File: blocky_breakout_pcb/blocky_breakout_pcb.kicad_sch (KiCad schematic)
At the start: 5 parts, among them J12 Conn_01x02_Pin

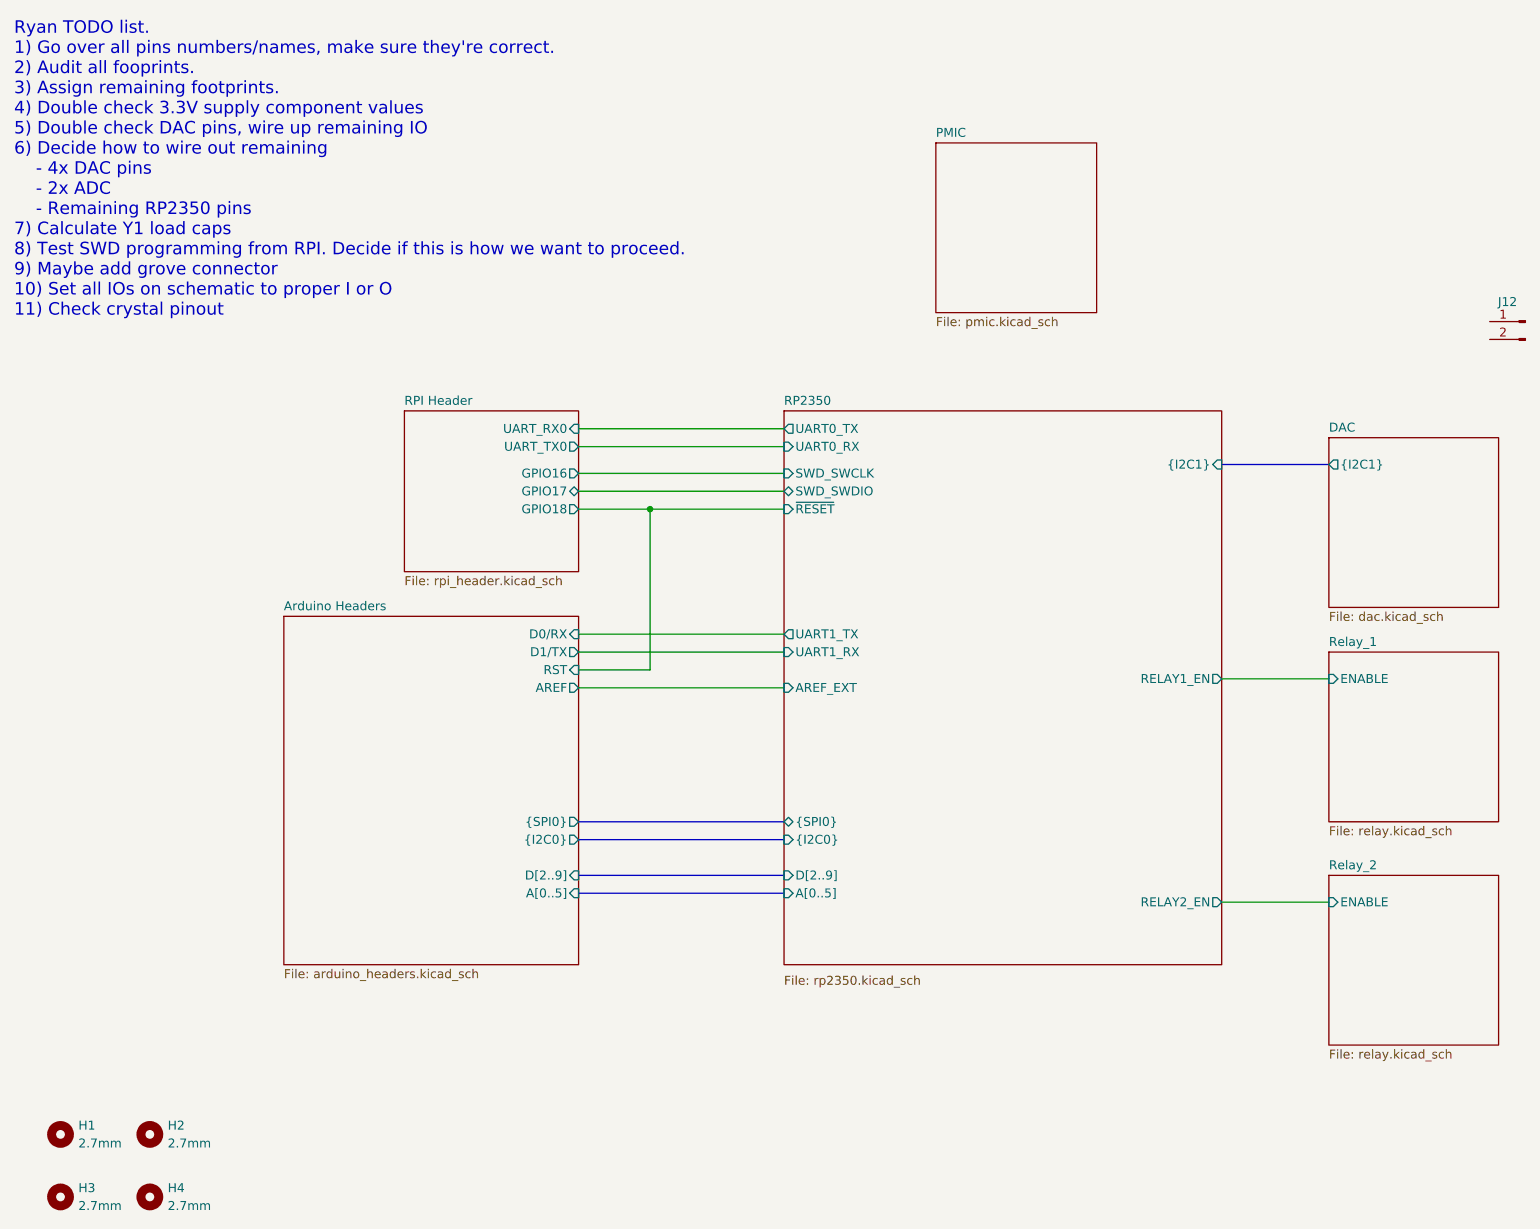
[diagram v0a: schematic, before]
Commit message: Layout nearly finished, entering part numbers
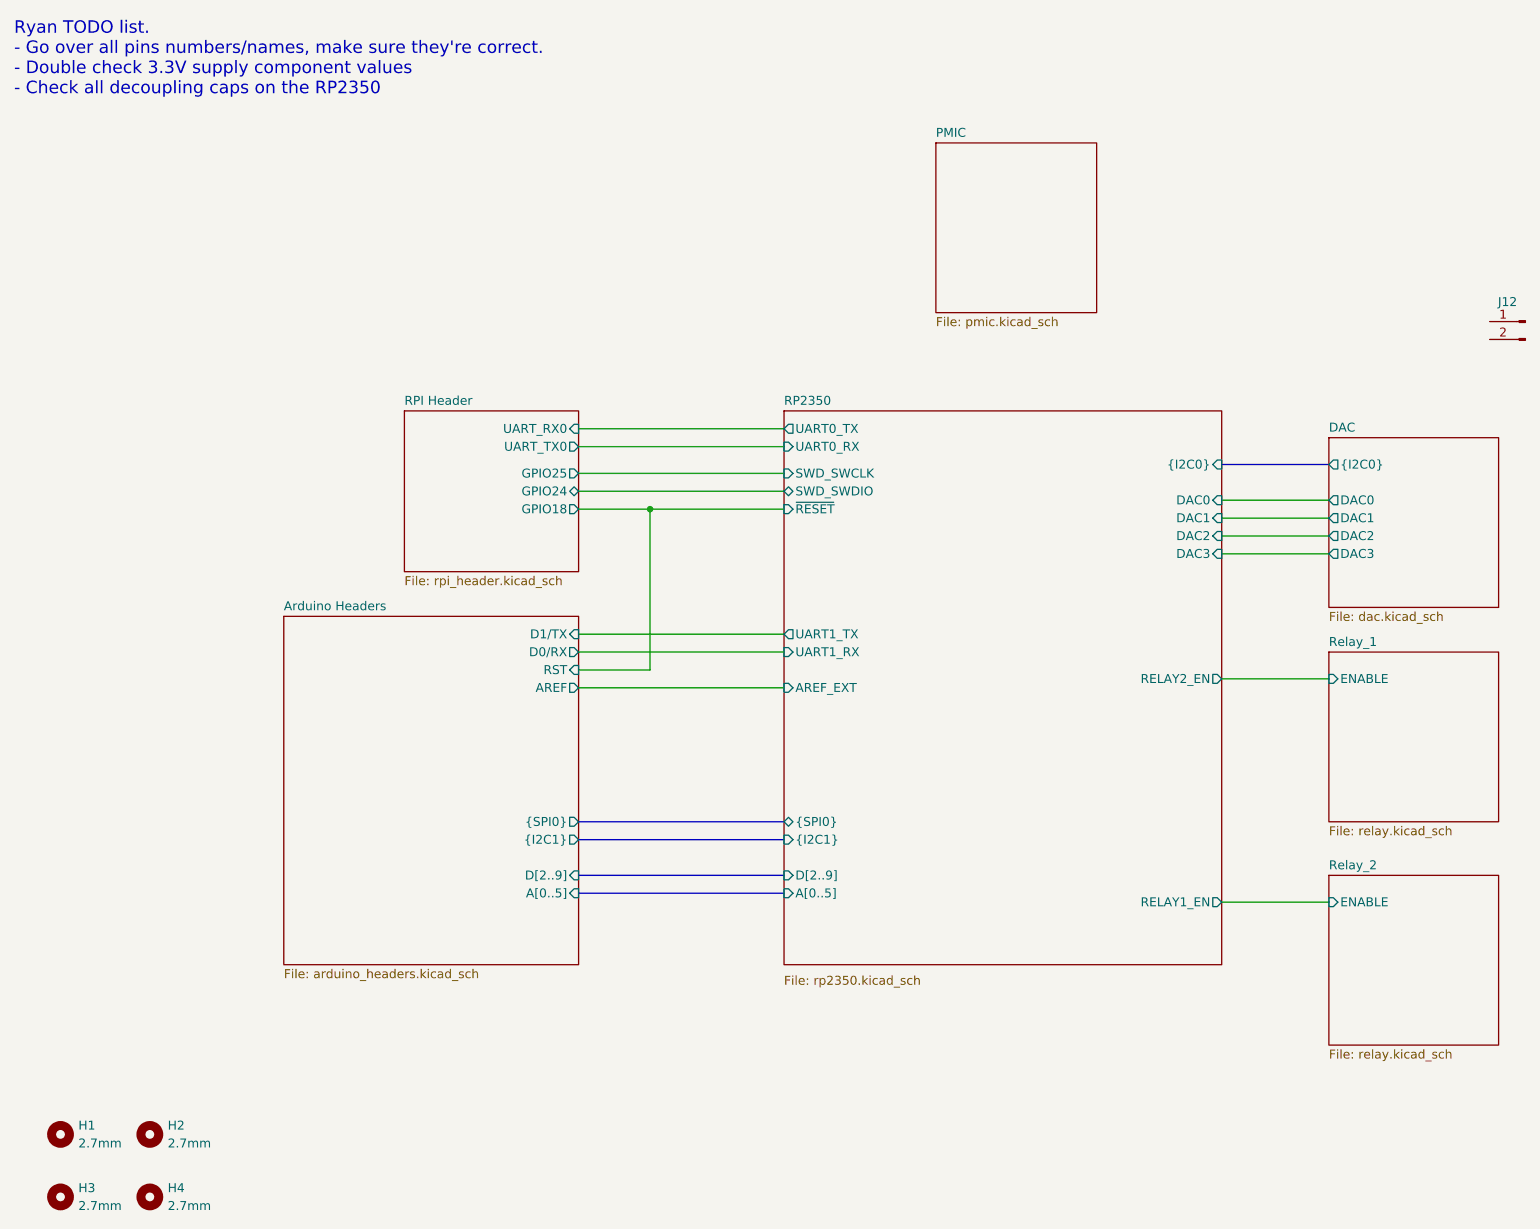
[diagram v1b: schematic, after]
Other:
- sheet Arduino Headers ports: added {I2C1}; removed {I2C0}
- sheet DAC ports: added DAC0, DAC1, DAC2, DAC3, {I2C0}; removed {I2C1}
- sheet RP2350 ports: added DAC0, DAC1, DAC2, DAC3; removed none
- sheet RPI Header ports: added GPIO24, GPIO25; removed GPIO16, GPIO17
- note added: "Ryan TODO list. - Go over all pins numbers/names, make sure they're correct. - Double check 3.3V supply component values - Check all decoupling caps on the RP2350"
- note removed: "Ryan TODO list. 1) Go over all pins numbers/names, make sure they're correct. 2) Audit all fooprints. 3) Assign remaining footprints. 4) Double check 3.3V supply component values 5) Double check DAC pins, wire up remaining IO 6) Decide how to wire out remaining - 4x DAC pins - 2x ADC - Remaining RP2350 pins 7) Calculate Y1 load caps 8) Test SWD programming from RPI. Decide if this is how we want 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"
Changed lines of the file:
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@@
 		(members "I2C1.SCL" "I2C1.SDA")
 	)
-	(text "Ryan TODO list.\n1) Go over all pins numbers/names, make sure they're correct.\n2) Audit all fooprints.\n3) Assign remaining footprints.\n4) Double check 3.3V supply component values\n5) Double check DAC pins, wire up remaining IO\n6) Decide how to wire out remaining \n	- 4x DAC pins\n	- 2x ADC\n	- Remaining RP2350 pins\n7) Calculate Y1 load caps\n8) Test SWD programming from RPI. Decide if this is how we want to proceed.\n9) Maybe add grove connector\n10) Set all IOs on schematic to proper I or O\n11) Check crystal pinout"
+	(text "Ryan TODO list.\n- Go over all pins numbers/names, make sure they're correct.\n- Double check 3.3V supply component values\n- Check all decoupling caps on the RP2350"
 		(exclude_from_sim no)
 		(at 16.256 15.748 0)
@@
 	(wire
 		(pts
-			(xy 96.52 102.87) (xy 125.73 102.87)
+			(xy 96.52 76.2) (xy 125.73 76.2)
 		)
 		(stroke
@@
 		)
 	)
-	(wire
+	(bus
 		(pts
-			(xy 96.52 76.2) (xy 125.73 76.2)
+			(xy 96.52 139.7) (xy 125.73 139.7)
 		)
 		(stroke
@@
 		)
 	)
-	(bus
+	(wire
 		(pts
-			(xy 96.52 139.7) (xy 125.73 139.7)
+			(xy 96.52 110.49) (xy 125.73 110.49)
 		)
 		(stroke
@@
 	(wire
 		(pts
-			(xy 96.52 110.49) (xy 125.73 110.49)
+			(xy 96.52 102.87) (xy 125.73 102.87)
 		)
 		(stroke
@@
 	(wire
 		(pts
+			(xy 96.52 105.41) (xy 125.73 105.41)
+		)
+		(stroke
+			(width 0)
+			(type default)
+		)
+	)
+	(wire
+		(pts
+			(xy 187.96 88.9) (xy 203.2 88.9)
+		)
+		(stroke
+			(width 0)
+			(type default)
+		)
+	)
+	(wire
+		(pts
 			(xy 96.52 82.55) (xy 125.73 82.55)
 		)
@@
 	(wire
 		(pts
-			(xy 96.52 105.41) (xy 125.73 105.41)
+			(xy 187.96 83.82) (xy 203.2 83.82)
+		)
+		(stroke
+			(width 0)
+			(type default)
+		)
+	)
+	(wire
+		(pts
+			(xy 187.96 86.36) (xy 203.2 86.36)
 		)
 		(stroke
@@
 		)
 	)
+	(wire
+		(pts
+			(xy 187.96 91.44) (xy 203.2 91.44)
+		)
+		(stroke
+			(width 0)
+			(type default)
+		)
+	)
 	(bus
 		(pts
@@
 			)
 		)
-		(pin "{I2C1}" output
+		(pin "{I2C0}" output
 			(at 203.2 78.74 180)
 			(effects
@@
 			)
 		)
+		(pin "DAC0" output
+			(at 203.2 83.82 180)
+			(effects
+				(font
+					(size 1.27 1.27)
+				)
+				(justify left)
+			)
+		)
+		(pin "DAC1" output
+			(at 203.2 86.36 180)
+			(effects
+				(font
+					(size 1.27 1.27)
+				)
+				(justify left)
+			)
+		)
+		(pin "DAC2" output
+			(at 203.2 88.9 180)
+			(effects
+				(font
+					(size 1.27 1.27)
+				)
+				(justify left)
+			)
+		)
+		(pin "DAC3" output
+			(at 203.2 91.44 180)
+			(effects
+				(font
+					(size 1.27 1.27)
+				)
+				(justify left)
+			)
+		)
 		(instances
 			(project "blocky_breakout_pcb"
@@
 			)
 		)
-		(pin "{I2C0}" input
+		(pin "{I2C1}" input
 			(at 125.73 132.08 180)
 			(effects
@@
 			)
 		)
-		(pin "{I2C1}" input
+		(pin "{I2C0}" input
 			(at 187.96 78.74 0)
 			(effects
@@
 			)
 		)
-		(pin "RELAY1_EN" output
+		(pin "RELAY2_EN" output
 			(at 187.96 109.22 0)
 			(effects
@@
 			)
 		)
-		(pin "RELAY2_EN" output
+		(pin "RELAY1_EN" output
 			(at 187.96 140.97 0)
 			(effects
@@
 			)
 		)
+		(pin "DAC3" input
+			(at 187.96 91.44 0)
+			(effects
+				(font
+					(size 1.27 1.27)
+				)
+				(justify right)
+			)
+		)
+		(pin "DAC0" input
+			(at 187.96 83.82 0)
+			(effects
+				(font
+					(size 1.27 1.27)
+				)
+				(justify right)
+			)
+		)
+		(pin "DAC1" input
+			(at 187.96 86.36 0)
+			(effects
+				(font
+					(size 1.27 1.27)
+				)
+				(justify right)
+			)
+		)
+		(pin "DAC2" input
+			(at 187.96 88.9 0)
+			(effects
+				(font
+					(size 1.27 1.27)
+				)
+				(justify right)
+			)
+		)
 		(instances
 			(project "blocky_breakout_pcb"
@@
 			)
 		)
-		(pin "D0{slash}RX" input
-			(at 96.52 102.87 0)
+		(pin "D0{slash}RX" output
+			(at 96.52 105.41 0)
 			(effects
 				(font
@@
 			)
 		)
-		(pin "D1{slash}TX" output
-			(at 96.52 105.41 0)
+		(pin "D1{slash}TX" input
+			(at 96.52 102.87 0)
 			(effects
 				(font
@@
 			)
 		)
-		(pin "{I2C0}" output
+		(pin "{I2C1}" output
 			(at 96.52 132.08 0)
 			(effects
@@
 			)
 		)
-		(pin "GPIO16" output
-			(at 96.52 80.01 0)
+		(pin "UART_RX0" input
+			(at 96.52 73.66 0)
 			(effects
 				(font
@@
 			)
 		)
-		(pin "GPIO17" bidirectional
-			(at 96.52 82.55 0)
+		(pin "UART_TX0" output
+			(at 96.52 76.2 0)
 			(effects
 				(font
@@
 			)
 		)
-		(pin "UART_RX0" input
-			(at 96.52 73.66 0)
+		(pin "GPIO18" output
+			(at 96.52 85.09 0)
 			(effects
 				(font
@@
 			)
 		)
-		(pin "UART_TX0" output
-			(at 96.52 76.2 0)
+		(pin "GPIO24" bidirectional
+			(at 96.52 82.55 0)
 			(effects
 				(font
@@
 			)
 		)
-		(pin "GPIO18" output
-			(at 96.52 85.09 0)
+		(pin "GPIO25" output
+			(at 96.52 80.01 0)
 			(effects
 				(font
